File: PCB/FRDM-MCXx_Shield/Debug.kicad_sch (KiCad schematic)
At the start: 14 parts, among them J6 Conn_01x04_Pin, J7 Conn_01x04_Pin, J8 Conn_01x04_Pin

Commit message: Updated PCB
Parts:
- renumbered D22 to D10, D23 to D11, D18 to D12, D24 to D13, D17 to D9
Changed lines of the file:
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@@
 		(dnp no)
 		(fields_autoplaced yes)
-		(property "Reference" "#PWR070"
+		(property "Reference" "#PWR032"
 			(at 54.61 187.96 0)
 			(effects
@@
 			(project "FRDM-MCXx_Shield"
 				(path "/bffc27af-f9e0-4cc8-b5dc-88d2faf26a17/1dfdf8f6-c624-48d2-b647-f547c6376b37"
-					(reference "#PWR070")
+					(reference "#PWR032")
 					(unit 1)
 				)
@@
 		(dnp no)
 		(fields_autoplaced yes)
-		(property "Reference" "#PWR044"
+		(property "Reference" "#PWR024"
 			(at 67.31 43.18 0)
 			(effects
@@
 			(project "FRDM-MCXx_Shield"
 				(path "/bffc27af-f9e0-4cc8-b5dc-88d2faf26a17/1dfdf8f6-c624-48d2-b647-f547c6376b37"
-					(reference "#PWR044")
+					(reference "#PWR024")
 					(unit 1)
 				)
@@
 		(dnp no)
 		(fields_autoplaced yes)
-		(property "Reference" "#PWR042"
+		(property "Reference" "#PWR028"
 			(at 67.31 95.25 0)
 			(effects
@@
 			(project "FRDM-MCXx_Shield"
 				(path "/bffc27af-f9e0-4cc8-b5dc-88d2faf26a17/1dfdf8f6-c624-48d2-b647-f547c6376b37"
-					(reference "#PWR042")
+					(reference "#PWR028")
 					(unit 1)
 				)
@@
 		(dnp no)
 		(fields_autoplaced yes)
-		(property "Reference" "#PWR069"
+		(property "Reference" "#PWR031"
 			(at 54.61 152.4 0)
 			(effects
@@
 			(project "FRDM-MCXx_Shield"
 				(path "/bffc27af-f9e0-4cc8-b5dc-88d2faf26a17/1dfdf8f6-c624-48d2-b647-f547c6376b37"
-					(reference "#PWR069")
+					(reference "#PWR031")
 					(unit 1)
 				)
@@
 		(dnp no)
 		(fields_autoplaced yes)
-		(property "Reference" "D24"
+		(property "Reference" "D13"
 			(at 60.96 173.9899 0)
 			(effects
@@
 			(project "FRDM-MCXx_Shield"
 				(path "/bffc27af-f9e0-4cc8-b5dc-88d2faf26a17/1dfdf8f6-c624-48d2-b647-f547c6376b37"
-					(reference "D24")
+					(reference "D13")
 					(unit 1)
 				)
@@
 		(dnp no)
 		(fields_autoplaced yes)
-		(property "Reference" "D23"
+		(property "Reference" "D11"
 			(at 60.96 104.1399 0)
 			(effects
@@
 			(project "FRDM-MCXx_Shield"
 				(path "/bffc27af-f9e0-4cc8-b5dc-88d2faf26a17/1dfdf8f6-c624-48d2-b647-f547c6376b37"
-					(reference "D23")
+					(reference "D11")
 					(unit 1)
 				)
@@
 		(dnp no)
 		(fields_autoplaced yes)
-		(property "Reference" "#PWR045"
+		(property "Reference" "#PWR026"
 			(at 67.31 68.58 0)
 			(effects
@@
 			(project "FRDM-MCXx_Shield"
 				(path "/bffc27af-f9e0-4cc8-b5dc-88d2faf26a17/1dfdf8f6-c624-48d2-b647-f547c6376b37"
-					(reference "#PWR045")
+					(reference "#PWR026")
 					(unit 1)
 				)
@@
 		(dnp no)
 		(fields_autoplaced yes)
-		(property "Reference" "D22"
+		(property "Reference" "D10"
 			(at 60.96 64.7699 0)
 			(effects
@@
 			(project "FRDM-MCXx_Shield"
 				(path "/bffc27af-f9e0-4cc8-b5dc-88d2faf26a17/1dfdf8f6-c624-48d2-b647-f547c6376b37"
-					(reference "D22")
+					(reference "D10")
 					(unit 1)
 				)
@@
 		(dnp no)
 		(fields_autoplaced yes)
-		(property "Reference" "D18"
+		(property "Reference" "D12"
 			(at 60.96 138.4299 0)
 			(effects
@@
 			(project "FRDM-MCXx_Shield"
 				(path "/bffc27af-f9e0-4cc8-b5dc-88d2faf26a17/1dfdf8f6-c624-48d2-b647-f547c6376b37"
-					(reference "D18")
+					(reference "D12")
 					(unit 1)
 				)
@@
 		(dnp no)
 		(fields_autoplaced yes)
-		(property "Reference" "D17"
+		(property "Reference" "D9"
 			(at 60.96 39.3699 0)
 			(effects
@@
 			(project "FRDM-MCXx_Shield"
 				(path "/bffc27af-f9e0-4cc8-b5dc-88d2faf26a17/1dfdf8f6-c624-48d2-b647-f547c6376b37"
-					(reference "D17")
+					(reference "D9")
 					(unit 1)
 				)
@@
 		(dnp no)
 		(fields_autoplaced yes)
-		(property "Reference" "#PWR068"
+		(property "Reference" "#PWR030"
 			(at 54.61 118.11 0)
 			(effects
@@
 			(project "FRDM-MCXx_Shield"
 				(path "/bffc27af-f9e0-4cc8-b5dc-88d2faf26a17/1dfdf8f6-c624-48d2-b647-f547c6376b37"
-					(reference "#PWR068")
+					(reference "#PWR030")
 					(unit 1)
 				)
@@
 		(dnp no)
 		(fields_autoplaced yes)
-		(property "Reference" "#PWR067"
+		(property "Reference" "#PWR027"
 			(at 54.61 78.74 0)
 			(effects
@@
 			(project "FRDM-MCXx_Shield"
 				(path "/bffc27af-f9e0-4cc8-b5dc-88d2faf26a17/1dfdf8f6-c624-48d2-b647-f547c6376b37"
-					(reference "#PWR067")
+					(reference "#PWR027")
 					(unit 1)
 				)
@@
 		(dnp no)
 		(fields_autoplaced yes)
-		(property "Reference" "#PWR043"
+		(property "Reference" "#PWR029"
 			(at 67.31 107.95 0)
 			(effects
@@
 			(project "FRDM-MCXx_Shield"
 				(path "/bffc27af-f9e0-4cc8-b5dc-88d2faf26a17/1dfdf8f6-c624-48d2-b647-f547c6376b37"
-					(reference "#PWR043")
+					(reference "#PWR029")
 					(unit 1)
 				)
@@
 		(dnp no)
 		(fields_autoplaced yes)
-		(property "Reference" "#PWR066"
+		(property "Reference" "#PWR025"
 			(at 54.61 53.34 0)
 			(effects
@@
 			(project "FRDM-MCXx_Shield"
 				(path "/bffc27af-f9e0-4cc8-b5dc-88d2faf26a17/1dfdf8f6-c624-48d2-b647-f547c6376b37"
-					(reference "#PWR066")
-					(unit 1)
-				)
+					(reference "#PWR025")
+					(unit 1)
+				)

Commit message: Fixed labeling
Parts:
- TP1, TP2, TP3, TP4, TP5, TP6: footprint 5000 -> SamacSys:5000
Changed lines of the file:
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@@
 			)
 		)
-		(property "Footprint" "5000"
+		(property "Footprint" "SamacSys:5000"
 			(at -25.07 181.61 0)
 			(effects
@@
 			)
 		)
-		(property "Footprint" "5000"
+		(property "Footprint" "SamacSys:5000"
 			(at -25.07 184.15 0)
 			(effects
@@
 			)
 		)
-		(property "Footprint" "5000"
+		(property "Footprint" "SamacSys:5000"
 			(at -25.07 179.07 0)
 			(effects
@@
 			)
 		)
-		(property "Footprint" "5000"
+		(property "Footprint" "SamacSys:5000"
 			(at -25.07 146.05 0)
 			(effects
@@
 			)
 		)
-		(property "Footprint" "5000"
+		(property "Footprint" "SamacSys:5000"
 			(at -25.07 143.51 0)
 			(effects
@@
 			)
 		)
-		(property "Footprint" "5000"
+		(property "Footprint" "SamacSys:5000"
 			(at -25.07 148.59 0)
 			(effects

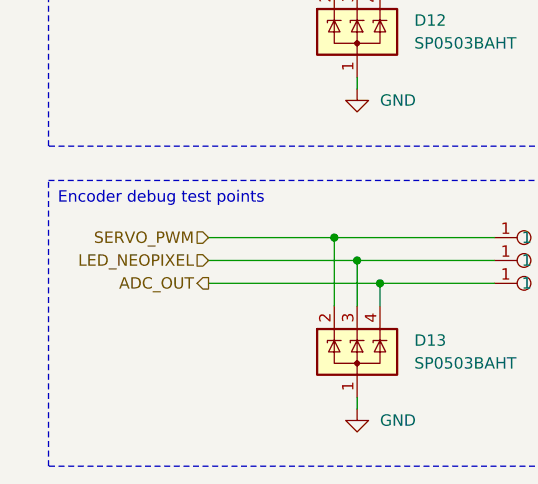
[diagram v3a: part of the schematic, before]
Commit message: Updated labeling and header positions
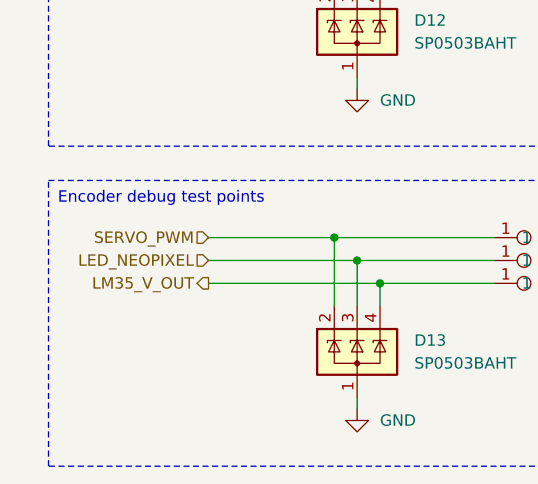
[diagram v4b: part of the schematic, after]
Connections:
- net ADC_OUT renamed LM35_V_OUT
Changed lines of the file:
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@@
 	(title_block
 		(title "Debug")
-		(date "2024-05-05")
+		(date "2024-05-20")
 		(rev "V2.0")
 		(company "HAN")
@@
 		)
 	)
-	(hierarchical_label "ADC_OUT"
+	(hierarchical_label "LM35_V_OUT"
 		(shape output)
 		(at 38.1 167.64 180)

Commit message: Updated V3.0
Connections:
- net SPI_CLK renamed SPI_SCK
- net WRITE_PROT renamed ~{EEPROM_WP}
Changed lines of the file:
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@@
 	(title_block
 		(title "Debug")
-		(date "2024-05-20")
+		(date "2024-06-17")
 		(rev "V3.0")
 		(company "HAN")
@@
 		)
 	)
-	(text_box "Encoder debug test points"
+	(text_box "Miscellaneous debug test points"
 		(exclude_from_sim no)
 		(at 20.32 156.21 0)
@@
 		)
 	)
-	(hierarchical_label "WRITE_PROT"
+	(hierarchical_label "~{EEPROM_WP}"
 		(shape input)
 		(at 38.1 77.47 180)
@@
 		)
 	)
-	(hierarchical_label "SPI_CLK"
+	(hierarchical_label "SPI_SCK"
 		(shape input)
 		(at 38.1 55.88 180)
